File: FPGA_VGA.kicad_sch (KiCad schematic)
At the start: 14 parts, among them J1 Conn_01x06, U1 Upduino_3.0

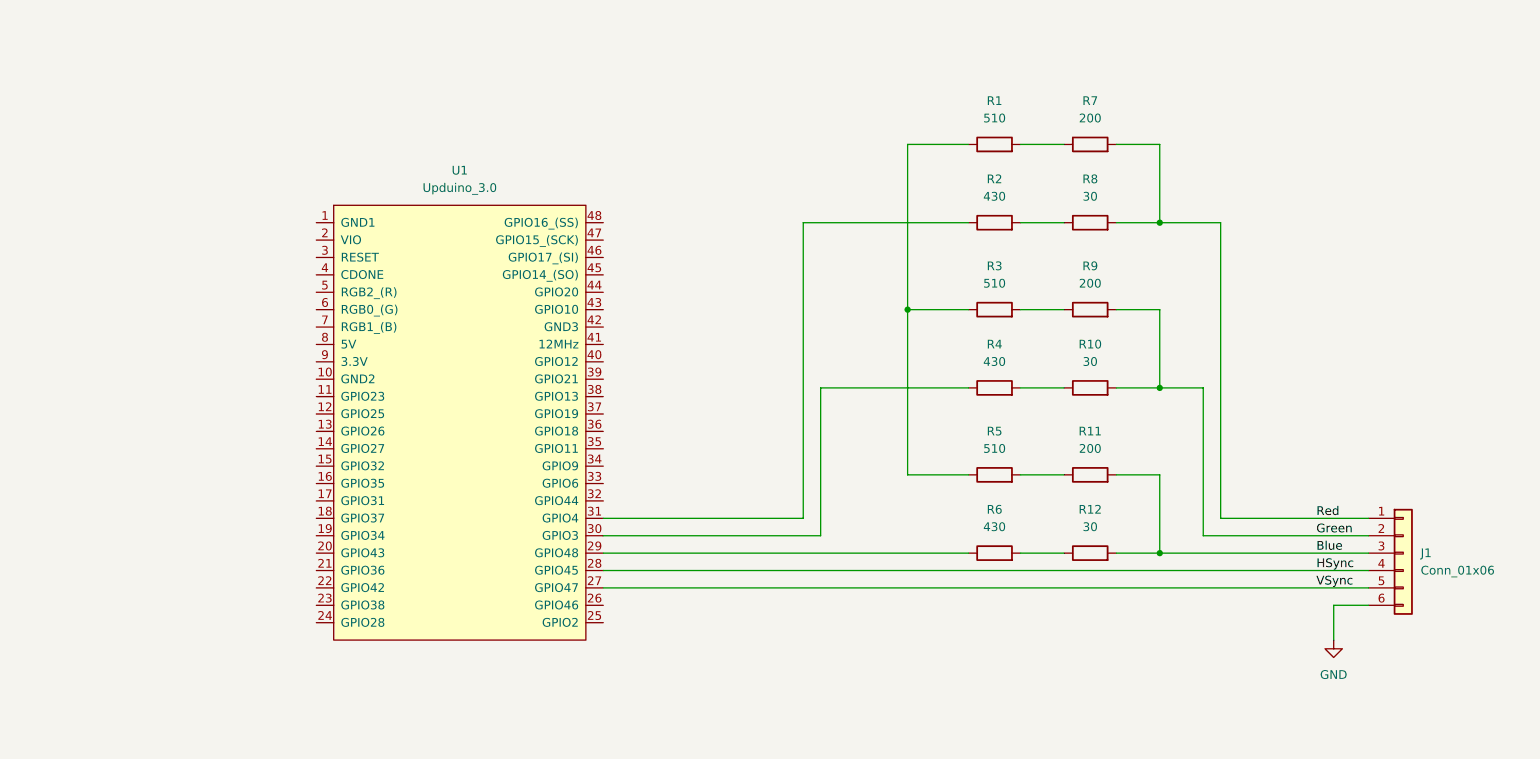
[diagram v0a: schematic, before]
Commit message: added oscillator, fix wiring to DAC and VGA conn
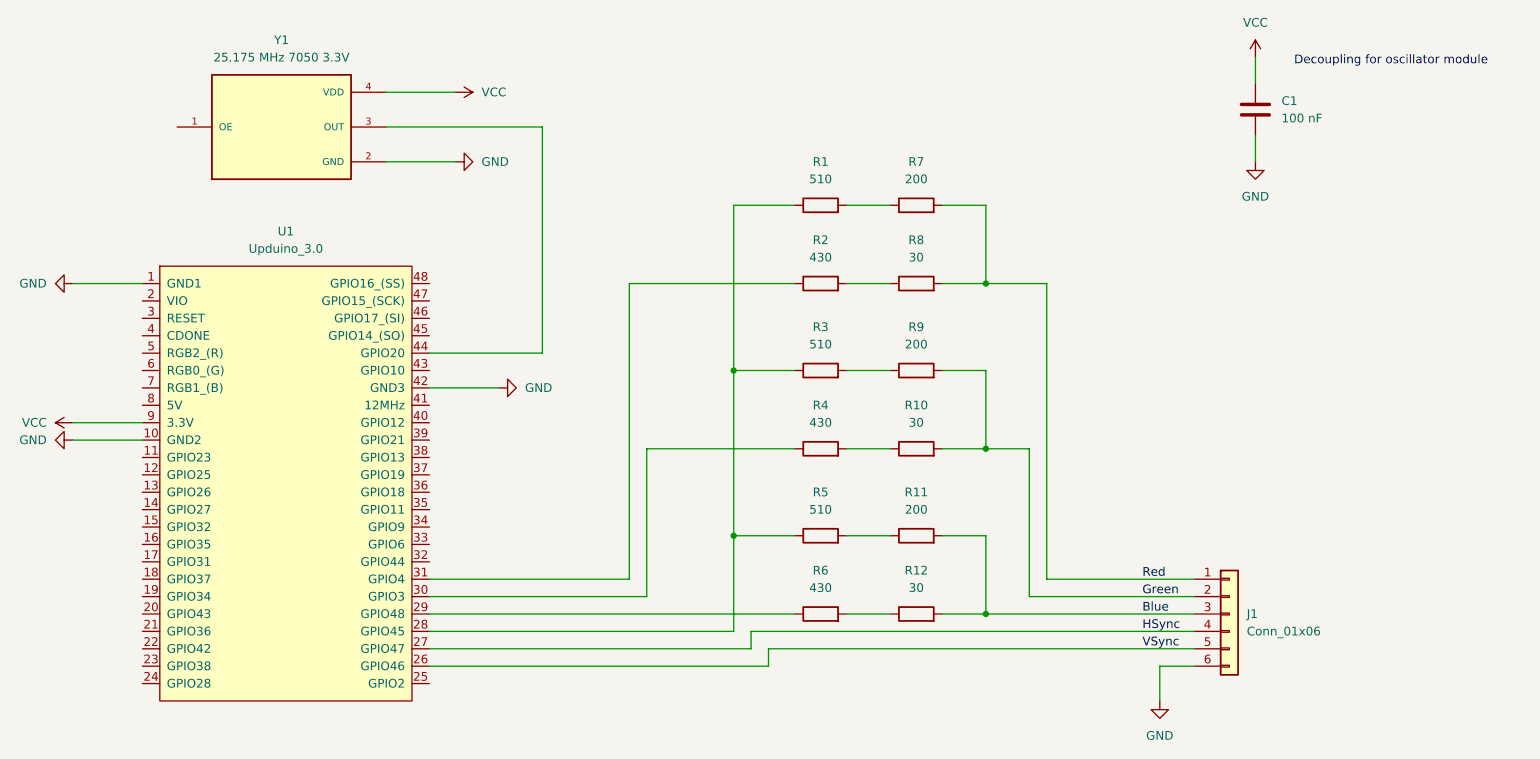
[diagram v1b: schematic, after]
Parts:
- added C1: 100 nF, symbol Device:C
- added Y1: 25.175 MHz 7050 3.3V, SIT8208AI-8F-33E-14.745600Y:OSC_SIT8208AI-8F-33E-14.745600Y, symbol SIT8208AI-8F-33E-14.745600Y:SIT8208AI-8F-33E-14.745600Y
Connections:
- net GND: now also U1.1 (GND1), U1.10 (GND2), U1.42 (GND3), C1.2, Y1.2 (GND)
- net HSync: now also U1.27 (GPIO47); no longer U1.28 (GPIO45)
- net VSync: now also U1.26 (GPIO46); no longer U1.27 (GPIO47)
- net at U1.44 (GPIO20): now also Y1.3 (OUT)
- net VCC: now reaches U1.9 (3.3V)
- net VCC: now also C1.1, Y1.4 (VDD)
- net at R1.1, R3.1, R5.1: now also U1.28 (GPIO45)
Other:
- note added: "Decoupling for oscillator module"
- moved on the sheet: J1, R1, R10, R11, R12, R2, R3, R4, R5, R6, R7, R8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
